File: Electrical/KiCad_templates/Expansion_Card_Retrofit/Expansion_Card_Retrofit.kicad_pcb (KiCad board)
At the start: 2 copper layers, 24 x 27.3 mm, 9 parts, among them P1 USB_C_Plug_USB2.0, U1 AP2112K-3.3

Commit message: First rough draft
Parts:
- added C1: 10uF, Capacitor_SMD:C_0603_1608Metric, F.Cu at (131.0, 86.8)
- added C10: 2u2, Capacitor_SMD:C_0402_1005Metric, F.Cu at (139.2, 71.2)
- added C11: 100n, Capacitor_SMD:C_0201_0603Metric, F.Cu at (143.1, 68.2)
- added C12: 100n, Capacitor_SMD:C_0201_0603Metric, F.Cu at (151.8, 93.8)
- added C13: 100n, Capacitor_SMD:C_0201_0603Metric, F.Cu at (143.8, 98.5)
- added C14: 2u2, Capacitor_SMD:C_0402_1005Metric, F.Cu at (142.0, 92.0)
- added C15: 2u2, Capacitor_SMD:C_0402_1005Metric, F.Cu at (142.0, 91.0)
- added C16: 2u2, Capacitor_SMD:C_0402_1005Metric, F.Cu at (136.5, 93.0)
- added C17: 100n, Capacitor_SMD:C_0201_0603Metric, F.Cu at (137.5, 93.2)
- added C18: 1n, Capacitor_SMD:C_0201_0603Metric, F.Cu at (143.6, 71.7)
- added C2: 10uF, Capacitor_SMD:C_0603_1608Metric, F.Cu at (131.5, 92.5)
- added C3: 15p, Capacitor_SMD:C_0201_0603Metric, F.Cu at (136.0, 101.0)
- added C4: 15p, Capacitor_SMD:C_0201_0603Metric, F.Cu at (134.1, 93.0)
- added C5: 100n, Capacitor_SMD:C_0201_0603Metric, F.Cu at (142.3, 61.9)
- added C6: 100n, Capacitor_SMD:C_0201_0603Metric, F.Cu at (142.6, 64.9)
- added C7: 2u2, Capacitor_SMD:C_0402_1005Metric, F.Cu at (139.2, 65.2)
- added C8: 2u2, Capacitor_SMD:C_0402_1005Metric, F.Cu at (139.2, 67.2)
- added C9: 2u2, Capacitor_SMD:C_0402_1005Metric, F.Cu at (139.2, 69.2)
- added D1: Green, LED_SMD:LED_0402_1005Metric, F.Cu at (130.5, 113.8)
- added D2: Orange, LED_SMD:LED_0402_1005Metric, F.Cu at (145.2, 88.5)
- added H1: MountingHole, MountingHole:MountingHole_2.2mm_M2, F.Cu at (129.0, 104.5)
- added H2: MountingHole, MountingHole:MountingHole_2.2mm_M2, F.Cu at (151.6, 104.5)
- added J1: Conn 10P, Connector_PinSocket_2.54mm:PinSocket_2x05_P2.54mm_Horizontal, F.Cu at (107.2, 87.4)
- added P1: USB_C_Plug_USB2.0, Expansion_Card:USB_C_Plug_Molex_105444, F.Cu at (140.3, 87.0)
- added Q1: DMG1012T, Package_TO_SOT_SMD:SOT-523, F.Cu at (157.9, 61.2)
- added Q2: Q_PMOS_SGD, Package_TO_SOT_SMD:SOT-523, F.Cu at (158.1, 65.8)
- added Q3: Q_NMOS_DGS, Package_TO_SOT_SMD:SOT-523, F.Cu at (158.1, 70.2)
- added R1: 5.1k, Resistor_SMD:R_0402_1005Metric, F.Cu at (135.2, 89.8)
- added R1: 5k1, Resistor_SMD:R_0402_1005Metric, F.Cu at (128.0, 63.5)
- added R10: 27R, Resistor_SMD:R_0201_0603Metric, F.Cu at (140.5, 90.5)
- added R11: 200R, Resistor_SMD:R_0603_1608Metric, F.Cu at (123.8, 70.2)
- added R12: 1R, Resistor_SMD:R_0402_1005Metric, F.Cu at (120.2, 62.5)
- added R13: 1K, Resistor_SMD:R_0402_1005Metric, F.Cu at (120.2, 64.5)
- added R14: R, Resistor_SMD:R_0402_1005Metric, F.Cu at (120.2, 66.5)
- added R15: 200K, Resistor_SMD:R_0402_1005Metric, F.Cu at (120.2, 68.5)
- added R16: 100K, Resistor_SMD:R_0402_1005Metric, F.Cu at (120.2, 70.5)
- added R17: 470R, Resistor_SMD:R_0402_1005Metric, F.Cu at (146.5, 88.5)
- added R2: R, Resistor_SMD:R_0402_1005Metric, F.Cu at (136.2, 99.3)
- added R3: 1K, Resistor_SMD:R_0402_1005Metric, F.Cu at (136.2, 97.0)
- added R4: 470R, Resistor_SMD:R_0402_1005Metric, F.Cu at (131.3, 66.5)
- added R5: 100K, Resistor_SMD:R_0402_1005Metric, F.Cu at (127.5, 70.2)
- added R6: 1K, Resistor_SMD:R_0402_1005Metric, F.Cu at (131.0, 70.0)
- added R7: 27R, Resistor_SMD:R_0201_0603Metric, F.Cu at (122.9, 65.4)
- added R8: 27R, Resistor_SMD:R_0201_0603Metric, F.Cu at (122.9, 67.2)
- added R9: 27R, Resistor_SMD:R_0201_0603Metric, F.Cu at (139.8, 90.5)
- added TP1: TestPoint, TestPoint:TestPoint_Pad_1.5x1.5mm, F.Cu at (134.6, 86.0)
- added TP2: TestPoint, TestPoint:TestPoint_Pad_1.5x1.5mm, B.Cu at (134.6, 86.0)
- added TP3: TestPoint, TestPoint:TestPoint_Pad_1.5x1.5mm, F.Cu at (146.0, 86.0)
- added TP4: TestPoint, TestPoint:TestPoint_Pad_1.5x1.5mm, B.Cu at (146.0, 86.0)
- added TP5: TestPoint, TestPoint:TestPoint_Pad_1.5x1.5mm, F.Cu at (130.0, 48.5)
- added TP6: TestPoint, TestPoint:TestPoint_Pad_1.5x1.5mm, F.Cu at (136.8, 48.5)
- added TP7: TestPoint, TestPoint:TestPoint_Pad_1.5x1.5mm, F.Cu at (133.2, 48.5)
- added U1: AP2112K-3.3, Package_TO_SOT_SMD:SOT-23-5, F.Cu at (131.2, 89.8)
- added U2: RP2040, Package_DFN_QFN:QFN-56-1EP_7x7mm_P0.4mm_EP3.2x3.2mm, B.Cu at (147.1, 93.8)
- added U3: W25Q16JVUXIQ, Package_SON:WSON-8-1EP_6x5mm_P1.27mm_EP3.4x4.3mm, B.Cu at (139.8, 97.4)
- added U4: RP2040, Package_DFN_QFN:QFN-56-1EP_7x7mm_P0.4mm_EP3.2x3.2mm, F.Cu at (147.1, 93.9)
- added U5: W25Q16JVUXIQ, Package_SON:WSON-8-1EP_6x5mm_P1.27mm_EP3.4x4.3mm, F.Cu at (139.7, 97.5)
- added U6: 74CBTLV3861, Package_DFN_QFN:DHVQFN-20-1EP_2.5x4.5mm_P0.5mm_EP1x3mm, F.Cu at (147.6, 100.5)
- added X1: 12MHz, Crystal:Crystal_SMD_0603-4Pin_6.0x3.5mm, F.Cu at (133.2, 97.0)
- C1, C2: value 10uF -> 10u; footprint Capacitor_SMD:C_0805_2012Metric -> Capacitor_SMD:C_0603_1608Metric
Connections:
- P1 pad A5: Net-(P1-PadA5) -> Net-(P1-CC)
- P1 pad A6: (no net) -> USB_DP
- P1 pad A7: (no net) -> USB_DN
- P1 pad B5: (no net) -> unconnected-(P1-VCONN-PadB5)
- U1 pad 4: (no net) -> unconnected-(U1-NC-Pad4)
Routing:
- net VBUS: track 0.00 -> 12.7 mm
- net /XR: track 0.00 -> 7.41 mm
- net +3V3: track 0.00 -> 6.83 mm
- net Net-(P1-PadA5): track 0.00 -> 5.54 mm
- net /Debug Probe Section/QSPI_SD3: track 0.00 -> 5.37 mm
- net Net-(U4-USB_DP): track 0.00 -> 5.33 mm
- net Net-(U4-USB_DM): track 0.00 -> 4.61 mm
- net /Debug Probe Section/QSPI_SCLK: track 0.00 -> 3.98 mm
- net XIN: track 0.00 -> 3.46 mm
- net USB_DP: track 0.00 -> 3.21 mm
- net USB_DN: track 0.00 -> 3.11 mm
- net +1V1: track 0.00 -> 2.49 mm
- net /Debug Probe Section/QSPI_SD0: track 0.00 -> 2.33 mm
- net /Debug Probe Section/LED_INT_EN: track 0.00 -> 1.49 mm
- net Net-(D2-A): track 0.00 -> 1.26 mm
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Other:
- board size 24 x 27.3 mm -> 26 x 69.5 mm
- net class Default removed

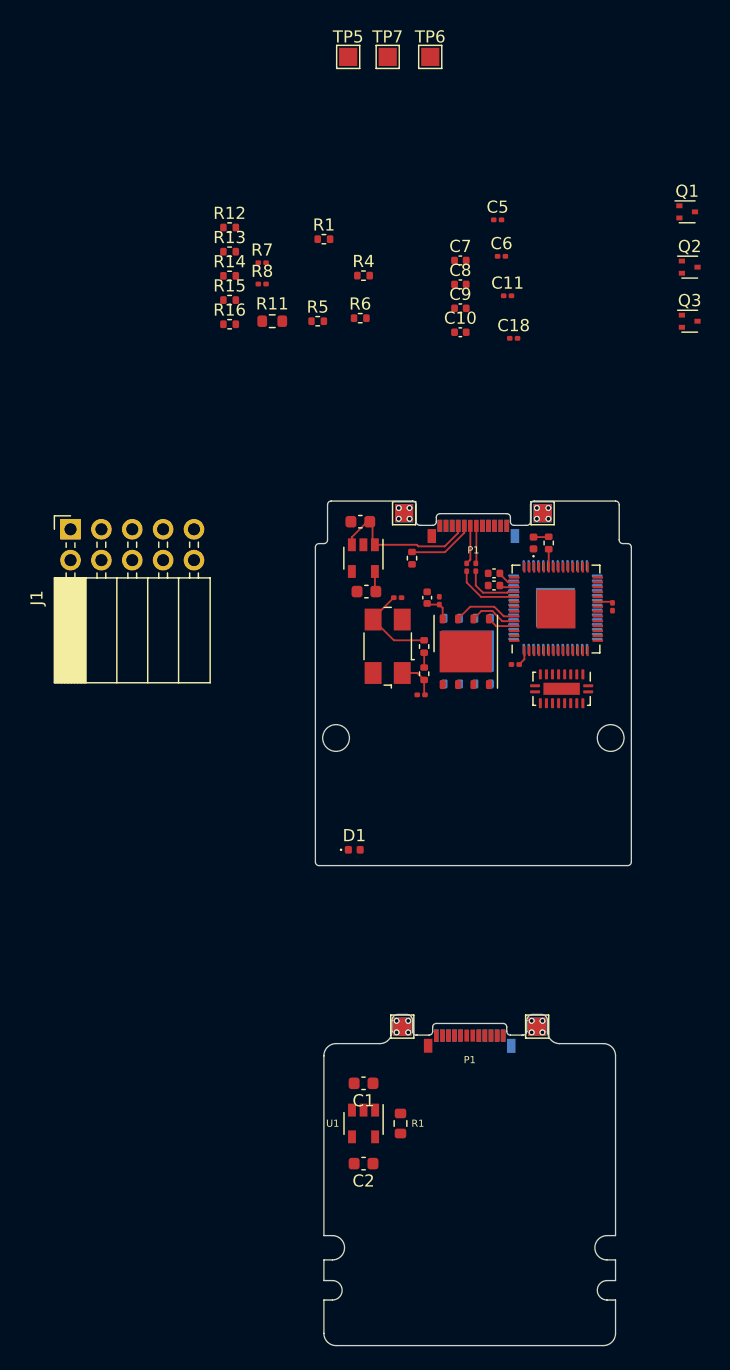
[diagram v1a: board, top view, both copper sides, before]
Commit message: Main layout of chip sections finished
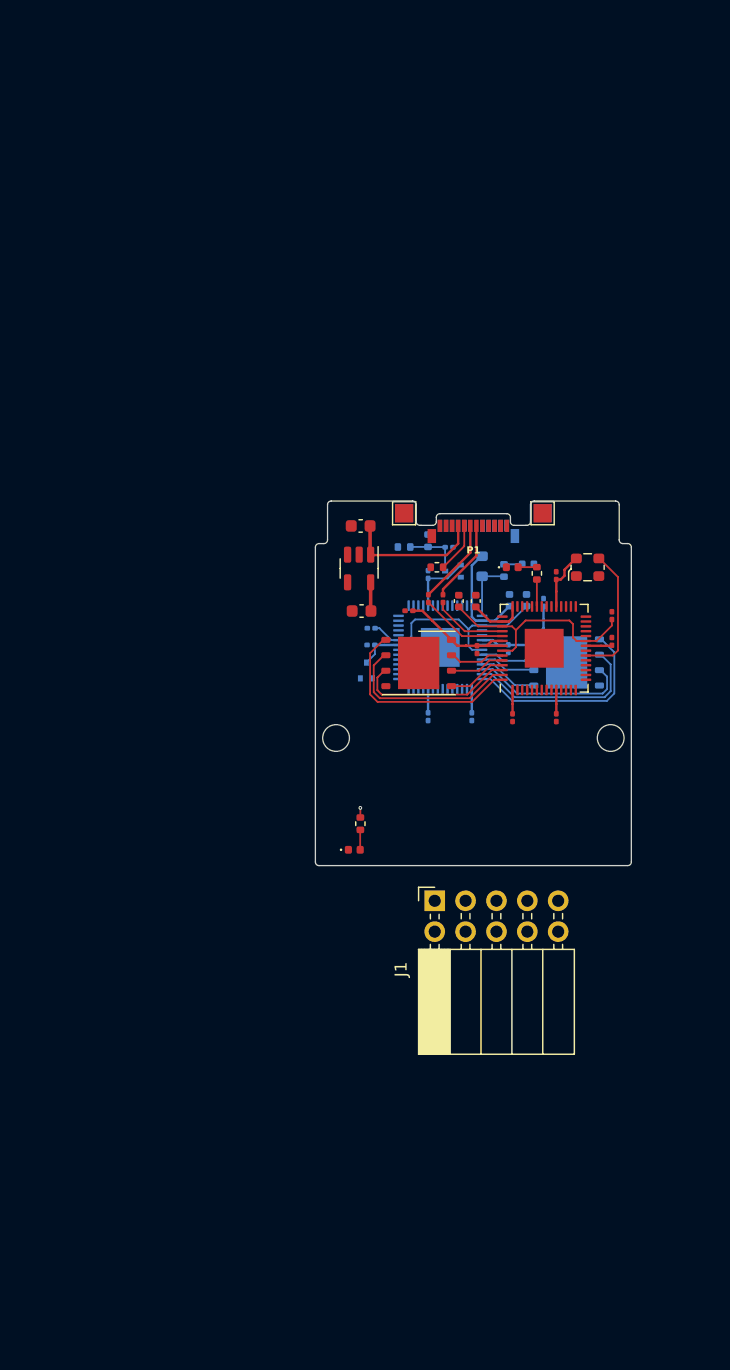
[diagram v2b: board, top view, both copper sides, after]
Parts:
- removed the C1 at (131.3, 133.0)
- removed the C1 at (131.0, 86.8)
- removed the C2 at (131.3, 139.6)
- removed the C2 at (131.5, 92.5)
- removed C3, C4: 15p, Capacitor_SMD:C_0201_0603Metric
- removed the P1 at (140.0, 129.0)
- removed Q3: Q_NMOS_DGS, Package_TO_SOT_SMD:SOT-523
- removed the R1 at (134.3, 136.3)
- removed the R1 at (135.2, 89.8)
- removed the R1 at (128.0, 63.5)
- removed R13, R3, R6: 1K, Resistor_SMD:R_0402_1005Metric
- removed R14, R2: R, Resistor_SMD:R_0402_1005Metric
- removed R5: 100K, Resistor_SMD:R_0402_1005Metric
- removed R7, R8: 27R, Resistor_SMD:R_0201_0603Metric
- removed the TP1 at (134.4, 128.3)
- removed the TP2 at (134.4, 128.3)
- removed the TP3 at (145.6, 128.3)
- removed the TP4 at (145.6, 128.3)
- removed TP5, TP6, TP7: TestPoint, TestPoint:TestPoint_Pad_1.5x1.5mm
- removed the U1 at (131.3, 136.3)
- removed the U1 at (131.2, 89.8)
- removed U6: 74CBTLV3861, Package_DFN_QFN:DHVQFN-20-1EP_2.5x4.5mm_P0.5mm_EP1x3mm
- added C1: 10u, Capacitor_SMD:C_0603_1608Metric, F.Cu at (131.0, 87.1)
- added C19: 100n, Capacitor_SMD:C_0201_0603Metric, F.Cu at (147.1, 102.9)
- added C2: 10u, Capacitor_SMD:C_0603_1608Metric, F.Cu at (131.1, 94.1)
- added C20: 100n, Capacitor_SMD:C_0201_0603Metric, F.Cu at (151.7, 96.6)
- added C21: 100n, Capacitor_SMD:C_0201_0603Metric, F.Cu at (147.1, 91.2)
- added C22: 100n, Capacitor_SMD:C_0201_0603Metric, B.Cu at (136.6, 102.8)
- added C23: 100n, Capacitor_SMD:C_0201_0603Metric, B.Cu at (131.9, 96.9)
- added C24: 100n, Capacitor_SMD:C_0201_0603Metric, B.Cu at (136.6, 91.1)
- added R1: 5k1, Resistor_SMD:R_0402_1005Metric, F.Cu at (137.3, 90.5)
- added U1: AP2112K-3.3, Package_TO_SOT_SMD:SOT-23-5, F.Cu at (130.9, 90.6)
- C10: value 2u2 -> 100n; footprint Capacitor_SMD:C_0402_1005Metric -> Capacitor_SMD:C_0201_0603Metric; moved to B.Cu
- C11, C18, C5, C6, C7, C8, C9, Q1, Q2, R11, R12, R15, R16: moved to B.Cu
- C16: value 2u2 -> 100n; footprint Capacitor_SMD:C_0402_1005Metric -> Capacitor_SMD:C_0201_0603Metric
- X1: value 12MHz -> ECS-2520MVLC-120-CM-TR; footprint Crystal:Crystal_SMD_0603-4Pin_6.0x3.5mm -> Oscillator:Oscillator_SMD_ECS_2520MV-xxx-xx-4Pin_2.5x2.0mm
- moved R4 45.1 mm to (131.0, 111.6), turned to -90 degrees
- moved J1 42.8 mm to (137.1, 117.9)
- moved Q2 42.5 mm to (131.5, 99.0), turned to 90 degrees
- moved R12 36.1 mm to (142.8, 90.8), turned to 90 degrees
- moved Q1 35.3 mm to (138.6, 90.8), turned to 180 degrees
- moved C5 35.2 mm to (131.9, 95.5), turned to 180 degrees
- moved C6 32.3 mm to (143.2, 97.2), turned to -90 degrees
- moved C10 31.6 mm to (140.2, 102.8), turned to -90 degrees
- moved C7 28.5 mm to (144.7, 93.2), turned to 90 degrees
- moved R11 26.5 mm to (141.0, 90.4), turned to -90 degrees
- moved C8 26.3 mm to (143.3, 93.2), turned to 90 degrees
- moved C11 25.4 mm to (146.1, 93.4), turned to 90 degrees
- moved R15 24.9 mm to (134.6, 88.8)
- moved R16 24.2 mm to (136.6, 88.3), turned to 90 degrees
- moved C9 21.8 mm to (144.8, 90.2)
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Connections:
- C10 pad 1: +3V3 -> /Development Board Section/3V3_DEV
- C11 pad 1: +3V3 -> /Development Board Section/3V3_DEV
- P1 pad B5: (no net) -> unconnected-(P1-VCONN-PadB5)
- Q2 pad 2: Net-(Q2-G) -> DEV_ENABLE
- U2 pad 20: XIN -> OSC_OUT
- U2 pad 21: XOUT -> unconnected-(U2-XOUT-Pad21)
- U2 pad 46: Net-(U2-USB_DM) -> unconnected-(U2-USB_DM-Pad46)
- U2 pad 47: Net-(U2-USB_DP) -> unconnected-(U2-USB_DP-Pad47)
- U3 pad 8: +3V3 -> /Development Board Section/3V3_DEV
- U4 pad 20: XIN -> OSC_OUT
- U4 pad 21: XOUT -> unconnected-(U4-XOUT-Pad21)
- U4 pad 6: UART1_TX -> unconnected-(U4-GPIO4-Pad6)
- U4 pad 7: UART1_RX -> unconnected-(U4-GPIO5-Pad7)
- X1 pad 1: XIN -> unconnected-(X1-Tri-State-Pad1)
- X1 pad 3: /XR -> OSC_OUT
- X1 pad 4: GND -> +3V3
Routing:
- net +1V1: track 2.49 -> 36.7 mm
- net /Development Board Section/3V3_DEV: track 0.00 -> 31.2 mm
- net +3V3: track 6.83 -> 28.4 mm
- net /Development Board Section/QSPI_SS: track 0.00 -> 17.1 mm
- net /Debug Probe Section/QSPI_SS: track 0.00 -> 17.1 mm
- net /Debug Probe Section/QSPI_SD1: track 0.00 -> 16.0 mm
- net /Development Board Section/QSPI_SD1: track 0.00 -> 16.0 mm
- net /Debug Probe Section/QSPI_SD2: track 0.00 -> 14.1 mm
- net /Development Board Section/QSPI_SD2: track 0.00 -> 14.1 mm
- net OSC_OUT: track 0.00 -> 11.1 mm
- net /XR: track 7.41 -> 0.00 mm
- net /Development Board Section/QSPI_SD0: track 0.00 -> 5.30 mm
- net /Development Board Section/ADC_VREF: track 0.00 -> 5.07 mm
- net Net-(Q1-D): track 0.00 -> 4.85 mm
- net /Development Board Section/QSPI_SD3: track 0.00 -> 4.66 mm
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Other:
- board size 26 x 69.5 mm -> 26 x 30 mm
- copper layers 2 -> 6

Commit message: Current state before flash footprint update
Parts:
- J1: footprint Connector_PinSocket_2.54mm:PinSocket_2x05_P2.54mm_Horizontal -> SnapEDA:AMPHENOL_89883-405LF
- moved J1 9.29 mm to (142.1, 110.1), turned to 180 degrees
- moved C17 0.44 mm to (135.3, 93.8), turned to 90 degrees
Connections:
- J1 pad 1: GPIO2 -> VBUS
- J1 pad 10: VBUS -> GPIO5
- J1 pad 2: GPIO3 -> +3V3
- J1 pad 3: GPIO4 -> GND
- J1 pad 4: GPIO5 -> GPIO2
- J1 pad 5: GND -> GPIO_ADC1
- J1 pad 6: GPIO_ADC0 -> GPIO3
- J1 pad 7: GPIO_ADC1 -> GPIO_ADC0
- J1 pad 8: GND -> GPIO4
- J1 pad 9: +3V3 -> GND
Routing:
- net VBUS: track 11.4 -> 28.3 mm, vias 0 -> 1
- net +3V3: track 28.4 -> 37.1 mm, vias 0 -> 6
- net /Development Board Section/GPIO_ADC3: track 0.00 -> 2.55 mm
- net GND: track 0.00 -> 1.85 mm, vias 0 -> 9
- net /Development Board Section/3V3_DEV: track 31.2 -> 32.7 mm, vias 0 -> 2
- added copper zone on In1.Cu, net +3V3
- added copper zone on In2.Cu, net /Development Board Section/3V3_DEV
- added copper zone on B.Cu, net GND
- added copper zone on F.Cu, net GND
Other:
- copper layers 6 -> 4

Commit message: First complete version
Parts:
- added Q3: Q_Dual_NPN_NPN_C2E2C1E1B1B2, digikey-footprints:SOT-363, F.Cu at (135.6, 103.5)
- added S1: JS102011SAQN, SnapEDA:SW_JS102011SAQN, F.Cu at (131.8, 112.6)
- U3, U5: footprint Package_SON:WSON-8-1EP_6x5mm_P1.27mm_EP3.4x4.3mm -> SnapEDA:IC_W25Q16JVUXIQ_TR
- moved D1 20.8 mm to (151.3, 114.2)
- moved R4 20.8 mm to (151.8, 112.1)
- moved R16 1.56 mm to (135.4, 89.3), turned to -90 degrees
- moved U3 1.53 mm to (146.6, 97.7)
- moved U5 1.51 mm to (137.3, 98.5)
- moved C18 1.48 mm to (136.8, 88.5), turned to 90 degrees
- moved C16 1.44 mm to (142.2, 102.5), turned to 180 degrees
- moved C9 1.38 mm to (146.2, 90.2)
- moved C24 1.10 mm to (135.6, 91.6), turned to 180 degrees
- moved R12 1.03 mm to (143.7, 90.2), turned to 0 degrees
- moved R15 0.95 mm to (133.8, 89.3), turned to 90 degrees
- moved C22 0.85 mm to (135.8, 102.5), turned to 180 degrees
- moved C5 0.58 mm to (131.9, 96.1)
- moved J1 0.57 mm to (142.7, 110.1)
- moved C11 0.53 mm to (146.6, 93.4)
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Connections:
- R15 pad 1: /Development Board Section/VSYS -> VBUS
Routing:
- net SWDIO: track 0.00 -> 31.9 mm, vias 0 -> 2
- net LED_EN: track 0.79 -> 31.5 mm
- net SWCLK: track 0.00 -> 28.2 mm, vias 0 -> 2
- net OSC_OUT: track 11.1 -> 38.0 mm, vias 0 -> 2
- net GPIO3: track 0.00 -> 19.7 mm, vias 0 -> 1
- net GPIO5: track 0.00 -> 18.3 mm, vias 0 -> 1
- net GPIO4: track 0.00 -> 16.8 mm, vias 0 -> 1
- net GPIO_ADC0: track 0.00 -> 16.4 mm, vias 0 -> 1
- net GPIO2: track 0.00 -> 16.0 mm, vias 0 -> 1
- net DEV_ENABLE: track 0.00 -> 14.7 mm, vias 0 -> 1
- net GPIO_ADC1: track 0.00 -> 14.3 mm, vias 0 -> 1
- net VBUS: track 28.3 -> 38.2 mm, vias 1 -> 2
- net /Development Board Section/QSPI_SS: track 17.1 -> 11.3 mm
- net /Development Board Section/QSPI_SD1: track 16.0 -> 10.2 mm
- net /Debug Probe Section/QSPI_SS: track 17.1 -> 11.4 mm
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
